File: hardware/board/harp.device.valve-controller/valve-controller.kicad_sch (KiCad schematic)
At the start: 0 parts

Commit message: route pcb
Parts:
- added J26: Conn_02x10_Odd_Even, Connector_PinHeader_2.54mm:PinHeader_2x10_P2.54mm_Vertical_SMD, symbol Connector_Generic:Conn_02x10_Odd_Even
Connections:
- new net +3.3V: J26.19 (Pin_19)
- new net +5V: J26.17 (Pin_17)
- new net GND: J26.10 (Pin_10), J26.12 (Pin_12), J26.14 (Pin_14), J26.16 (Pin_16), J26.18 (Pin_18), J26.2 (Pin_2), J26.20 (Pin_20), J26.4 (Pin_4), J26.6 (Pin_6), J26.8 (Pin_8)
- new net Harp Core RP2040 + Isolated USB/GPIO0: J26.1 (Pin_1)
- new net Harp Core RP2040 + Isolated USB/GPIO1: J26.3 (Pin_3)
- new net Harp Core RP2040 + Isolated USB/GPIO2: J26.5 (Pin_5)
- new net Harp Core RP2040 + Isolated USB/GPIO3: J26.7 (Pin_7)
- new net Harp Core RP2040 + Isolated USB/GPIO4: J26.9 (Pin_9)
- new net Harp Core RP2040 + Isolated USB/GPIO5: J26.11 (Pin_11)
- new net Harp Core RP2040 + Isolated USB/GPIO6: J26.13 (Pin_13)
- new net Harp Core RP2040 + Isolated USB/GPIO7: J26.15 (Pin_15)
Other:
- sheet Harp Core RP2040 + Isolated USB ports: added GPIO0, GPIO1, GPIO2, GPIO3, GPIO4, GPIO5, GPIO6, GPIO7; removed EXT_TRIG0, EXT_TRIG1, EXT_TRIG2, EXT_TRIG3, POKE_IN0, POKE_IN1, POKE_IN2, POKE_IN3
- note removed: "* Valve Power Input & device power input * RF Isolation * Flyback diodes"
- note removed: "Level shift 5VTTL to 3.3VCMOS with: SN74LV1T34"

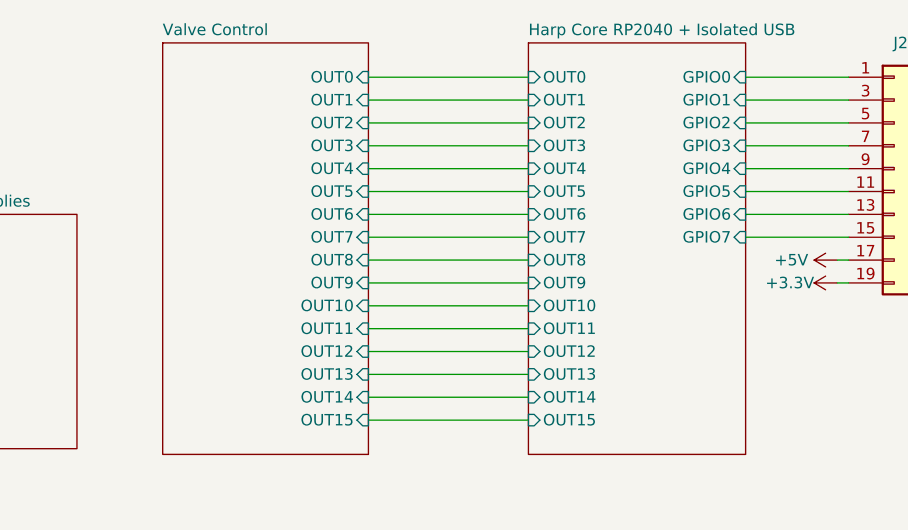
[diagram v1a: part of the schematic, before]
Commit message: update pcb power supply
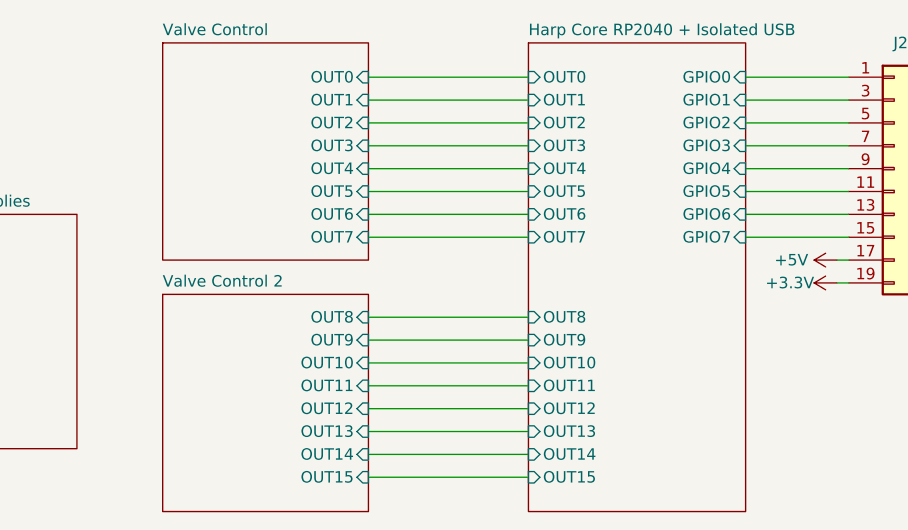
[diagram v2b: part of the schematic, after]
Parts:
- J26: Manufacturer (none) -> Molex; Manufacturer Number (none) -> 0015910200
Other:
- added sheet Valve Control 2 (valve_ctrl2.kicad_sch)
- sheet Valve Control ports: added none; removed OUT10, OUT11, OUT12, OUT13, OUT14, OUT15, OUT8, OUT9
